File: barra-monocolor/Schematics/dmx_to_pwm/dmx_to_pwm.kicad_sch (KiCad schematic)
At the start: 19 parts, among them J1 Conn_01x05_Socket, J4 PJ-031D, Q1 BD237, Q2 BD237, Q3 BD237, Q4 BD237, U1 SN75176AP, U3 PC817

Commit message: added pdf schematics
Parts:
- removed C3: 10uF, Capacitor_THT:CP_Radial_Tantal_D5.5mm_P2.50mm, symbol Device:C_Polarized
- removed J4: PJ-031D, PJ031D, symbol PJ-031D:PJ-031D
- added J2: RJ45 IN, symbol Connector:RJ45
- added J3: RJ45 OUT, symbol Connector:RJ45
- C6: value 100nF -> 10uF
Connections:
- net GND: now also J2.6, J2.7, J2.8, J3.6, J3.7, J3.8
- net VCC: now also J2.3, J2.4, J2.5, J3.3, J3.4, J3.5
- net +5V renamed +4V BUCKET
- net DATA+_IN renamed DATA+
- net DATA+: now also J2.1, J3.1
- net DATA-_IN renamed DATA-
- net DATA-: now also J2.2, J3.2

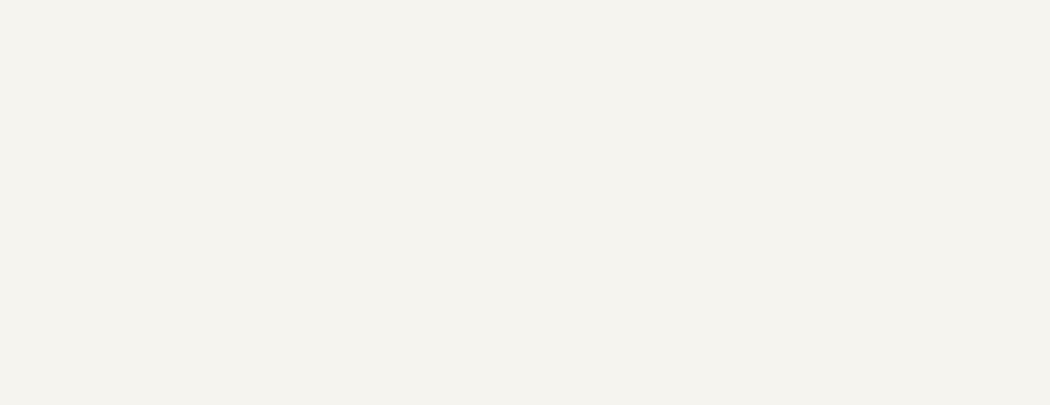
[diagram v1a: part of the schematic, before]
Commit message: Added drivers to monochrome schematics
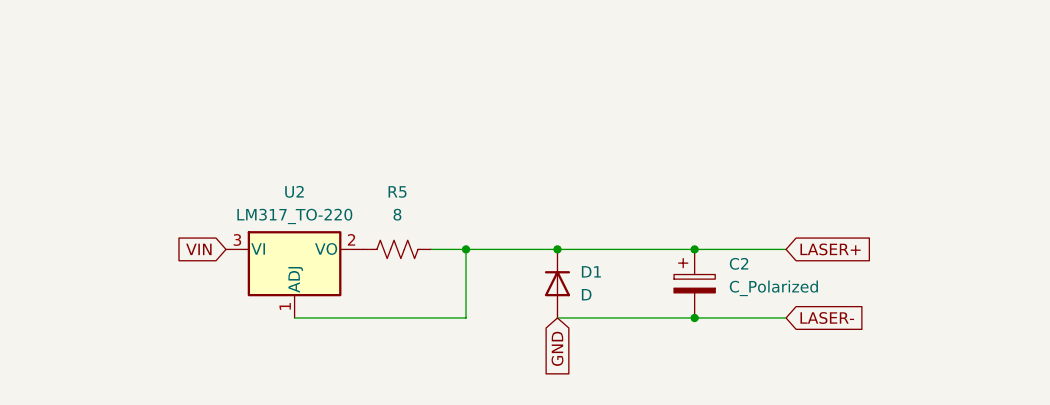
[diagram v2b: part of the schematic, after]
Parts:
- added C2: C_Polarized, symbol Device:C_Polarized
- added D1: D, symbol Device:D
- added R5: 8, symbol Device:R_US
- added U2: LM317_TO-220, Package_TO_SOT_THT:TO-220-3_Vertical, symbol Regulator_Linear:LM317_TO-220
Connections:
- net GND: now also C2.2, D1.2 (A)
- new net: R5.1, U2.2 (VO)
- new net LASER+: C2.1, D1.1 (K), R5.2, U2.1 (ADJ)
- new net VIN: U2.3 (VI)

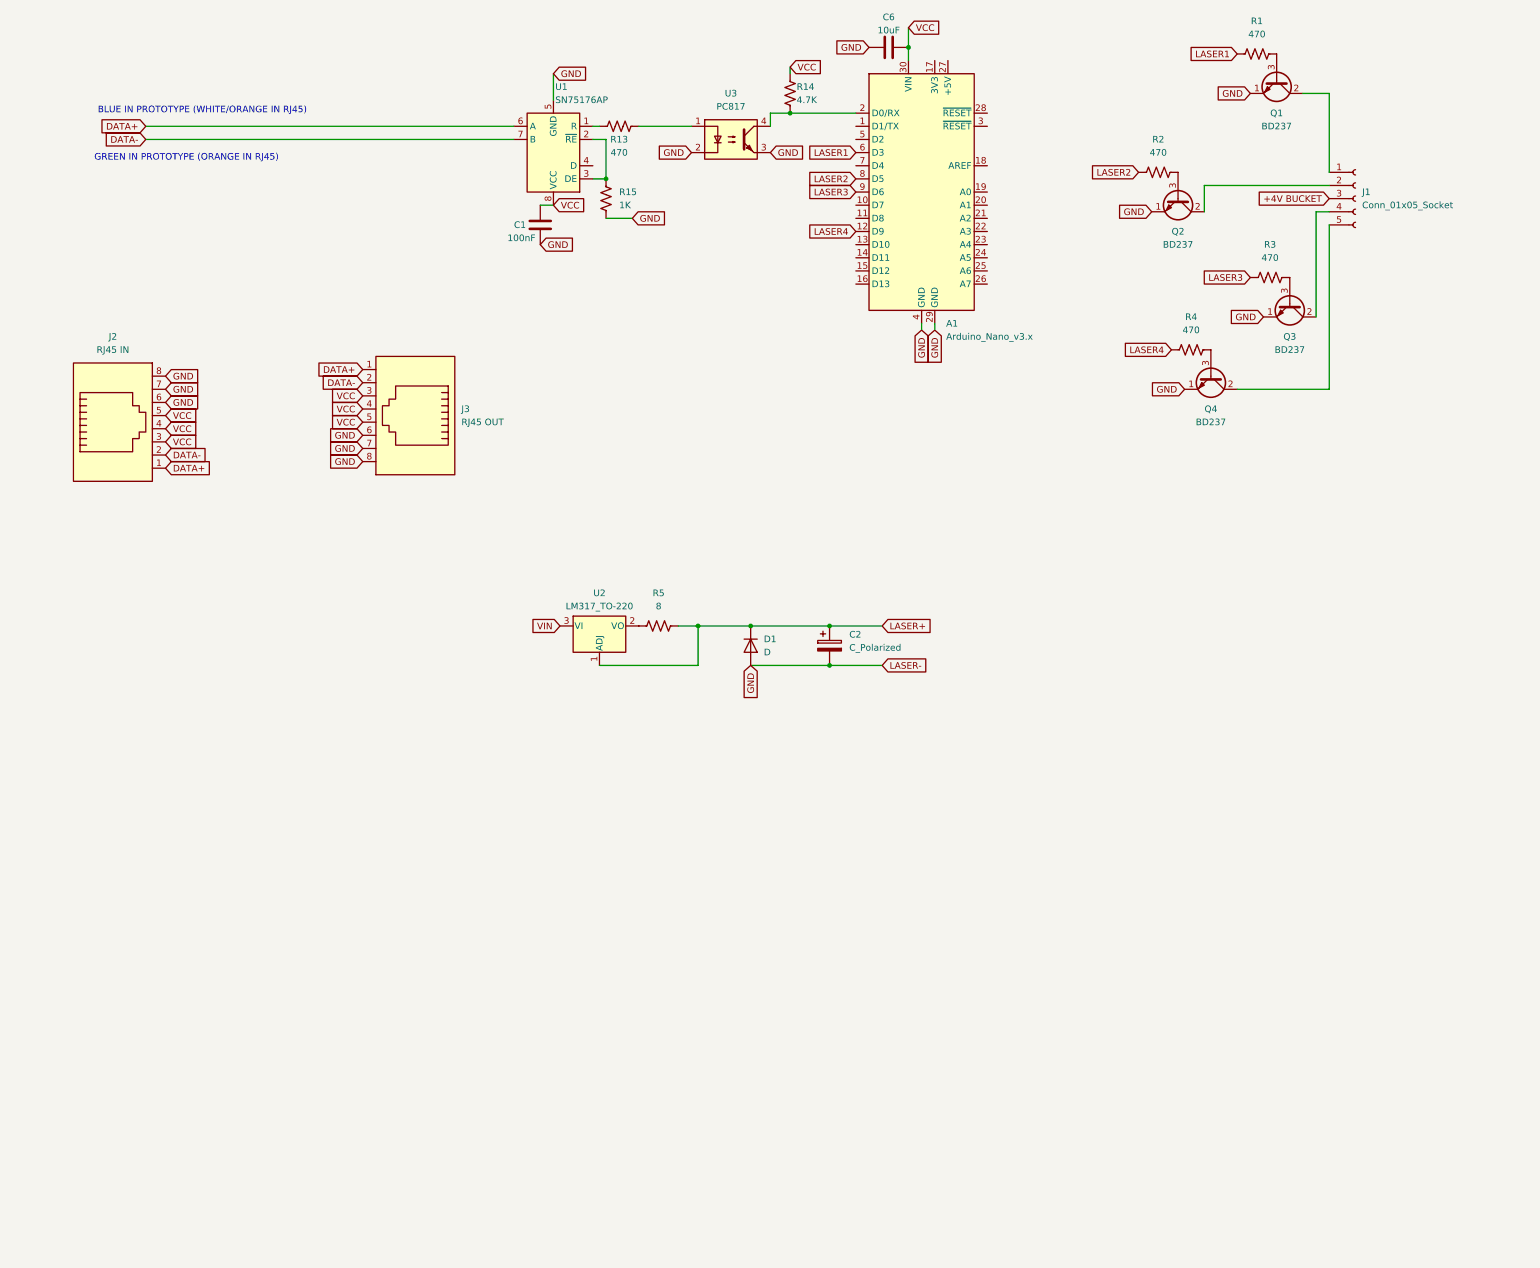
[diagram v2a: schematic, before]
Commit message: updated schematics
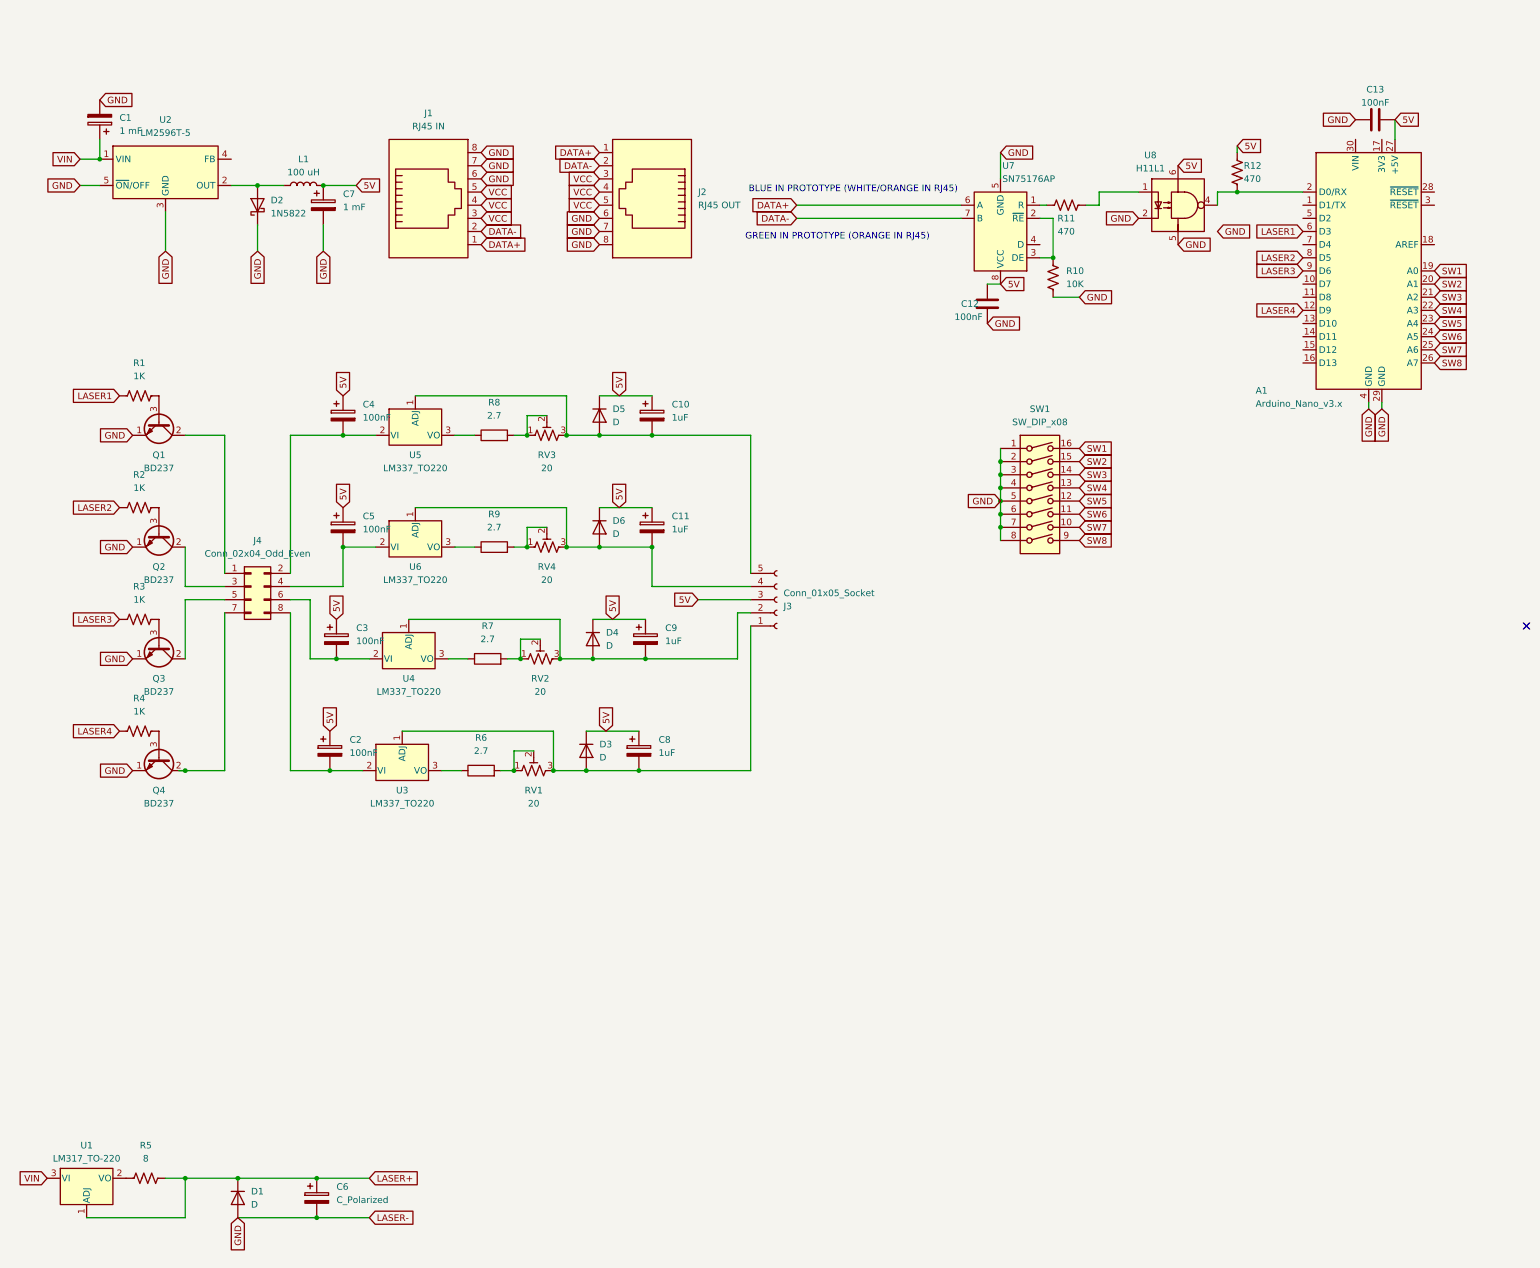
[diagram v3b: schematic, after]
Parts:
- removed C1: 100nF, Capacitor_THT:C_Disc_D3.0mm_W2.0mm_P2.50mm, symbol Device:C
- removed C6: 10uF, symbol Device:C
- removed J1: Conn_01x05_Socket, symbol Connector:Conn_01x05_Socket
- removed J3: RJ45 OUT, symbol Connector:RJ45
- removed R13: 470, Resistor_THT:R_Axial_DIN0204_L3.6mm_D1.6mm_P7.62mm_Horizontal, symbol Device:R_US
- removed R14: 4.7K, Resistor_THT:R_Axial_DIN0204_L3.6mm_D1.6mm_P7.62mm_Horizontal, symbol Device:R_US
- removed R15: 1K, symbol Device:R_US
- removed U1: SN75176AP, Package_DIP:DIP-8_W7.62mm, symbol Interface_UART:SN75176AP
- removed U2: LM317_TO-220, Package_TO_SOT_THT:TO-220-3_Vertical, symbol Regulator_Linear:LM317_TO-220
- removed U3: PC817, Package_DIP:DIP-4_W7.62mm, symbol Isolator:PC817
- added C1, C7: 1 mF, symbol Device:C_Polarized
- added C10, C11, C8, C9: 1uF, symbol Device:C_Polarized
- added C12: 100nF, Capacitor_THT:C_Disc_D3.0mm_W2.0mm_P2.50mm, symbol Device:C
- added C13: 100nF, symbol Device:C
- added C3, C4, C5: 100nF, symbol Device:C_Polarized
- added C6: C_Polarized, symbol Device:C_Polarized
- added D2: 1N5822, Diode_THT:D_DO-201AD_P15.24mm_Horizontal, symbol Diode:1N5822
- added D3, D4, D5, D6: D, symbol Device:D
- added J1: RJ45 IN, symbol Connector:RJ45
- added J3: Conn_01x05_Socket, symbol Connector:Conn_01x05_Socket
- added J4: Conn_02x04_Odd_Even, symbol Connector_Generic:Conn_02x04_Odd_Even
- added L1: 100 uH, symbol Device:L
- added R10: 10K, symbol Device:R_US
- added R11, R12: 470, Resistor_THT:R_Axial_DIN0204_L3.6mm_D1.6mm_P7.62mm_Horizontal, symbol Device:R_US
- added R6, R7, R8, R9: 2.7, symbol Device:R
- added RV1, RV2, RV3, RV4: 20, symbol Device:R_Potentiometer_Trim_US
- added SW1: SW_DIP_x08, symbol Switch:SW_DIP_x08
- added U1: LM317_TO-220, Package_TO_SOT_THT:TO-220-3_Vertical, symbol Regulator_Linear:LM317_TO-220
- added U2: LM2596T-5, Package_TO_SOT_THT:TO-220-5_P3.4x3.7mm_StaggerOdd_Lead3.8mm_Vertical, symbol Regulator_Switching:LM2596T-5
- added U3, U4, U5, U6: LM337_TO220, Package_TO_SOT_THT:TO-220-3_Vertical, symbol Regulator_Linear:LM337_TO220
- added U7: SN75176AP, Package_DIP:DIP-8_W7.62mm, symbol Interface_UART:SN75176AP
- added U8: H11L1, symbol Isolator:H11L1
- C2: value C_Polarized -> 100nF
- J2: value RJ45 IN -> RJ45 OUT
- R1, R2, R3, R4: value 470 -> 1K
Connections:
- net DATA+: now also J1.1, U7.6 (A)
- net DATA-: now also J1.2, U7.7 (B)
- net GND: now also C1.2, C12.2, C13.1, C6.2, C7.2, D2.1 (K), J1.6, J1.7, J1.8, R10.2, SW1.1, SW1.2, SW1.3, SW1.4, SW1.5, SW1.6, SW1.7, SW1.8, U2.3 (GND), U2.5 (~{ON}/OFF), U7.5 (GND), U8.2, U8.5; no longer C2.2
- net LASER+: now also C6.1, U1.1 (ADJ); no longer C2.1
- net VCC: now also J1.3, J1.4, J1.5; no longer A1.30 (VIN)
- net VIN: now also C1.1, U1.3 (VI), U2.1 (VIN)
- net at Q3.2 (C): now also J4.5 (Pin_5)
- net at A1.2 (D0/RX): now also R12.2, U8.4
- net SW1: now reaches A1.19 (A0)
- net SW1: now also SW1.16
- net SW2: now reaches A1.20 (A1)
- net SW2: now also SW1.15
- net SW3: now reaches A1.21 (A2)
- net SW3: now also SW1.14
- net SW4: now reaches A1.22 (A3)
- net SW4: now also SW1.13
- net SW5: now reaches A1.23 (A4)
- net SW5: now also SW1.12
- net SW6: now reaches A1.24 (A5)
- net SW6: now also SW1.11
- net SW7: now reaches A1.25 (A6)
- net SW7: now also SW1.10
- net SW8: now reaches A1.26 (A7)
- net SW8: now also SW1.9
- net 5V: now reaches A1.27 (+5V)
- net 5V: now also C2.1, C10.1, C11.1, C12.1, C13.2, C3.1, C4.1, C5.1, C7.1, C8.1, C9.1, D3.1 (K), D4.1 (K), D5.1 (K), D6.1 (K), J3.3 (Pin_3), L1.2, R12.1, U7.8 (VCC), U8.6
- net at R5.1: now also U1.2 (VO)
- net at Q4.2 (C): now also J4.7 (Pin_7)
- net at Q1.2 (C): now also J4.1 (Pin_1)
- net at Q2.2 (C): now also J4.3 (Pin_3)
- new net: C11.2, D6.2 (A), J3.4 (Pin_4), RV4.3, U6.1 (ADJ)
- new net: C9.2, D4.2 (A), J3.2 (Pin_2), RV2.3, U4.1 (ADJ)
- new net: R7.1, U4.3 (VO)
- new net: R7.2, RV2.1, RV2.2
- new net: R10.1, U7.2 (~{RE}), U7.3 (DE)
- new net: C8.2, D3.2 (A), J3.1 (Pin_1), RV1.3, U3.1 (ADJ)
- new net: D2.2 (A), L1.1, U2.2 (OUT)
- new net: C3.2, J4.6 (Pin_6), U4.2 (VI)
- new net: R11.1, U7.1 (R)
- new net: R11.2, U8.1
- new net: R9.1, U6.3 (VO)
- new net: R9.2, RV4.1, RV4.2
- new net: R6.1, U3.3 (VO)
- new net: R6.2, RV1.1, RV1.2
- new net: C4.2, J4.2 (Pin_2), U5.2 (VI)
- new net: C5.2, J4.4 (Pin_4), U6.2 (VI)
- new net: C2.2, J4.8 (Pin_8), U3.2 (VI)
- new net: C10.2, D5.2 (A), J3.5 (Pin_5), RV3.3, U5.1 (ADJ)
- new net: R8.1, U5.3 (VO)
- new net: R8.2, RV3.1, RV3.2
- no-connect marks 0 -> 1

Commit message: updated rj45
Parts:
- J1: value RJ45 IN -> RJ45; footprint (none) -> Connector_RJ:RJ45_Amphenol_54602-x08_Horizontal
- J2: value RJ45 OUT -> RJ45
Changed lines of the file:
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@@
+	)
+	(symbol
+		(lib_id "Connector:RJ45")
+		(at 130.81 48.26 180)
+		(unit 1)
+		(exclude_from_sim no)
+		(in_bom yes)
+		(on_board yes)
+		(dnp no)
+		(fields_autoplaced yes)
+		(property "Reference" "J2"
+			(at 139.7 48.2599 0)
+			(effects
+				(font
+					(size 1.27 1.27)
+				)
+				(justify right)
+			)
+		)
+		(property "Value" "RJ45"
+			(at 139.7 50.7999 0)
+			(effects
+				(font
+					(size 1.27 1.27)
+				)
+				(justify right)
+			)
+		)
+		(property "Footprint" ""
+			(at 130.81 48.895 90)
+			(effects
+				(font
+					(size 1.27 1.27)
+				)
+				(hide yes)
+			)
+		)
+		(property "Datasheet" "~"
+			(at 130.81 48.895 90)
+			(effects
+				(font
+					(size 1.27 1.27)
+				)
+				(hide yes)
+			)
+		)
+		(property "Description" "RJ connector, 8P8C (8 positions 8 connected)"
+			(at 130.81 48.26 0)
+			(effects
+				(font
+					(size 1.27 1.27)
+				)
+				(hide yes)
+			)
+		)
+		(pin "5"
+		)
+		(pin "7"
+		)
+		(pin "3"
+		)
+		(pin "2"
+		)
+		(pin "1"
+		)
+		(pin "8"
+		)
+		(pin "6"
+		)
+		(pin "4"
+		)
+		(instances
+			(project ""
+				(path "/fe39f169-33b8-46fd-886b-c754b4eb741b"
+					(reference "J2")
+					(unit 1)
+				)
+			)
+		)
 	)
 	(symbol
@@
 				(path "/fe39f169-33b8-46fd-886b-c754b4eb741b"
 					(reference "Q2")
+					(unit 1)
+				)
+			)
+		)
+	)
+	(symbol
+		(lib_id "Connector:RJ45")
+		(at 87.63 50.8 0)
+		(unit 1)
+		(exclude_from_sim no)
+		(in_bom yes)
+		(on_board yes)
+		(dnp no)
+		(fields_autoplaced yes)
+		(property "Reference" "J1"
+			(at 87.63 33.02 0)
+			(effects
+				(font
+					(size 1.27 1.27)
+				)
+			)
+		)
+		(property "Value" "RJ45"
+			(at 87.63 35.56 0)
+			(effects
+				(font
+					(size 1.27 1.27)
+				)
+			)
+		)
+		(property "Footprint" "Connector_RJ:RJ45_Amphenol_54602-x08_Horizontal"
+			(at 87.63 50.165 90)
+			(effects
+				(font
+					(size 1.27 1.27)
+				)
+				(hide yes)
+			)
+		)
+		(property "Datasheet" "~"
+			(at 87.63 50.165 90)
+			(effects
+				(font
+					(size 1.27 1.27)
+				)
+				(hide yes)
+			)
+		)
+		(property "Description" "RJ connector, 8P8C (8 positions 8 connected)"
+			(at 87.63 50.8 0)
+			(effects
+				(font
+					(size 1.27 1.27)
+				)
+				(hide yes)
+			)
+		)
+		(pin "3"
+		)
+		(pin "2"
+		)
+		(pin "1"
+		)
+		(pin "6"
+		)
+		(pin "7"
+		)
+		(pin "8"
+		)
+		(pin "5"
+		)
+		(pin "4"
+		)
+		(instances
+			(project ""
+				(path "/fe39f169-33b8-46fd-886b-c754b4eb741b"
+					(reference "J1")
 					(unit 1)
 				)
@@
 	)
 	(symbol
-		(lib_id "Connector:RJ45")
-		(at 130.81 48.26 180)
-		(unit 1)
-		(exclude_from_sim no)
-		(in_bom yes)
-		(on_board yes)
-		(dnp no)
-		(fields_autoplaced yes)
-		(property "Reference" "J2"
-			(at 139.7 48.2599 0)
-			(effects
-				(font
-					(size 1.27 1.27)
-				)
-				(justify right)
-			)
-		)
-		(property "Value" "RJ45 OUT"
-			(at 139.7 50.7999 0)
-			(effects
-				(font
-					(size 1.27 1.27)
-				)
-				(justify right)
-			)
-		)
-		(property "Footprint" ""
-			(at 130.81 48.895 90)
-			(effects
-				(font
-					(size 1.27 1.27)
-				)
-				(hide yes)
-			)
-		)
-		(property "Datasheet" "~"
-			(at 130.81 48.895 90)
-			(effects
-				(font
-					(size 1.27 1.27)
-				)
-				(hide yes)
-			)
-		)
-		(property "Description" "RJ connector, 8P8C (8 positions 8 connected)"
-			(at 130.81 48.26 0)
-			(effects
-				(font
-					(size 1.27 1.27)
-				)
-				(hide yes)
-			)
-		)
-		(pin "1"
-		)
-		(pin "8"
-		)
-		(pin "4"
-		)
-		(pin "6"
-		)
-		(pin "7"
-		)
-		(pin "5"
-		)
-		(pin "2"
-		)
-		(pin "3"
-		)
-		(instances
-			(project "dmx_to_pwm"
-				(path "/fe39f169-33b8-46fd-886b-c754b4eb741b"
-					(reference "J2")
-					(unit 1)
-				)
-			)
-		)
-	)
-	(symbol
 		(lib_id "Regulator_Linear:LM337_TO220")
 		(at 82.55 160.02 0)
@@
 					(unit 1)
 				)
-			)
-		)
-	)
-	(symbol
-		(lib_id "Connector:RJ45")
-		(at 87.63 50.8 0)
-		(unit 1)
-		(exclude_from_sim no)
-		(in_bom yes)
-		(on_board yes)
-		(dnp no)
-		(fields_autoplaced yes)
-		(property "Reference" "J1"
-			(at 87.63 33.02 0)
-			(effects
-				(font
-					(size 1.27 1.27)
-				)
-			)
-		)
-		(property "Value" "RJ45 IN"
-			(at 87.63 35.56 0)
-			(effects
-				(font
-					(size 1.27 1.27)
-				)
-			)
-		)
-		(property "Footprint" ""
-			(at 87.63 50.165 90)
-			(effects
-				(font
-					(size 1.27 1.27)
-				)
-				(hide yes)
-			)
-		)
-		(property "Datasheet" "~"
-			(at 87.63 50.165 90)
-			(effects
-				(font
-					(size 1.27 1.27)
-				)
-				(hide yes)
-			)
-		)
-		(property "Description" "RJ connector, 8P8C (8 positions 8 connected)"
-			(at 87.63 50.8 0)
-			(effects
-				(font
-					(size 1.27 1.27)
-				)
-				(hide yes)
-			)
-		)
-		(pin "1"
-		)
-		(pin "8"
-		)
-		(pin "4"
-		)
-		(pin "6"
-		)
-		(pin "7"
-		)
-		(pin "5"
-		)
-		(pin "2"
-		)
-		(pin "3"
-		)
-		(instances
-			(project "dmx_to_pwm"
-				(path "/fe39f169-33b8-46fd-886b-c754b4eb741b"
-					(reference "J1")
-					(unit 1)
-				)
